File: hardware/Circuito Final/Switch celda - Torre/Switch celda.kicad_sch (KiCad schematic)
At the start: 30 parts, among them Q1 MMBT2222A, Q2 MMBT2907A, Q3 MMBT2222A

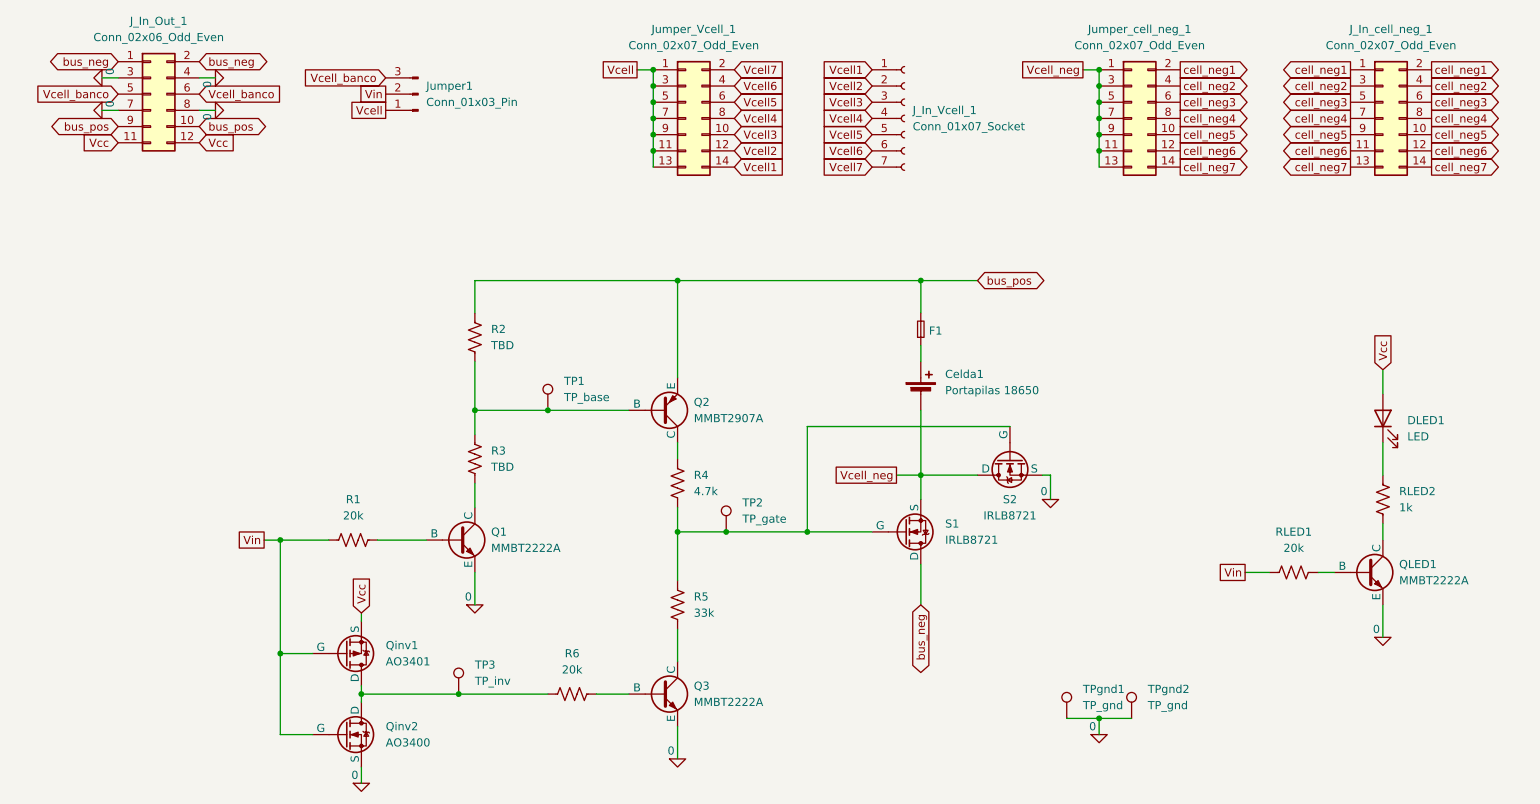
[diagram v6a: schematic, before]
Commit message: Eliminación del pin de señal de control para todo el banco y correcciones menores a la placa
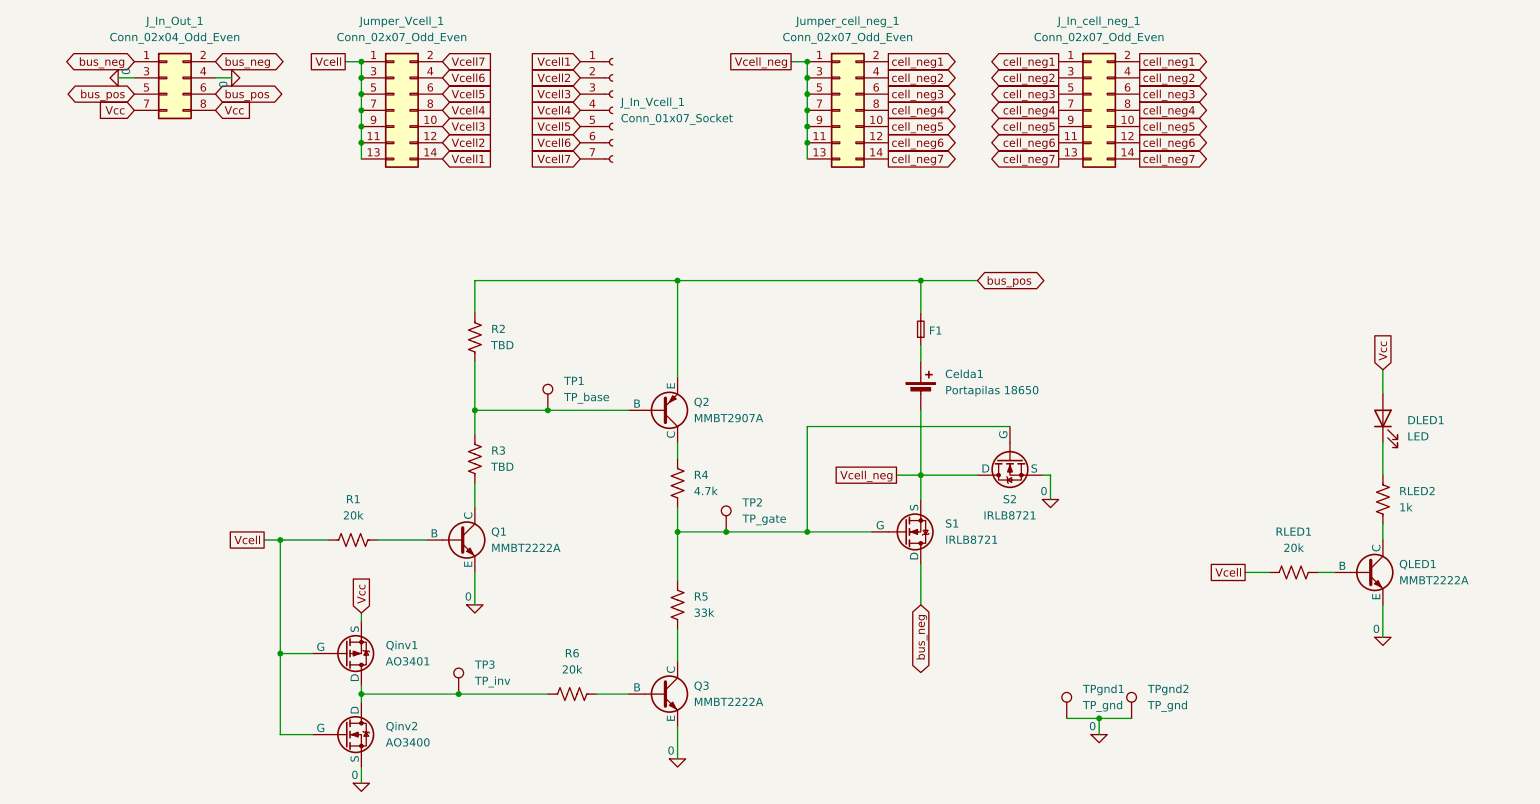
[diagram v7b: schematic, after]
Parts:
- removed J_In_Out_1: Conn_02x06_Odd_Even, Connector_PinSocket_2.54mm:PinSocket_2x06_P2.54mm_Vertical, symbol Connector_Generic:Conn_02x06_Odd_Even
- removed Jumper1: Conn_01x03_Pin, Connector_PinHeader_2.54mm:PinHeader_1x03_P2.54mm_Vertical, symbol Connector:Conn_01x03_Pin
- added J_In_Out_1: Conn_02x04_Odd_Even, Connector_PinSocket_2.54mm:PinSocket_2x04_P2.54mm_Vertical, symbol Connector_Generic:Conn_02x04_Odd_Even
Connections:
- net Vin is gone; now on net Vcell: Qinv1.2 (G), Qinv2.2 (G), R1.1, RLED1.1
- net 0: now also J_In_Out_1.3 (Pin_3), J_In_Out_1.4 (Pin_4)
- net Vcc: now also J_In_Out_1.7 (Pin_7), J_In_Out_1.8 (Pin_8)
- net bus_neg: now also J_In_Out_1.1 (Pin_1), J_In_Out_1.2 (Pin_2)
- net bus_pos: now also J_In_Out_1.5 (Pin_5), J_In_Out_1.6 (Pin_6)
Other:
- moved on the sheet: J_In_Vcell_1, J_In_cell_neg_1, Jumper_Vcell_1, Jumper_cell_neg_1

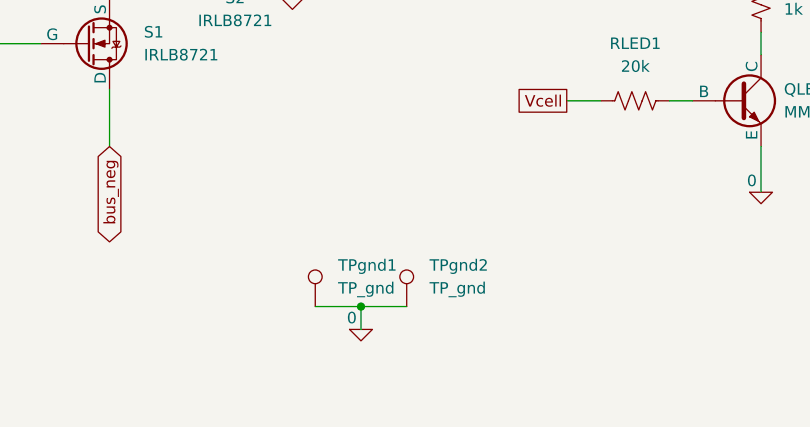
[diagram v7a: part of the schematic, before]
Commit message: Reemplazo de la vía por un resistor SMD de 0 ohm y corrección de los errores de DRC
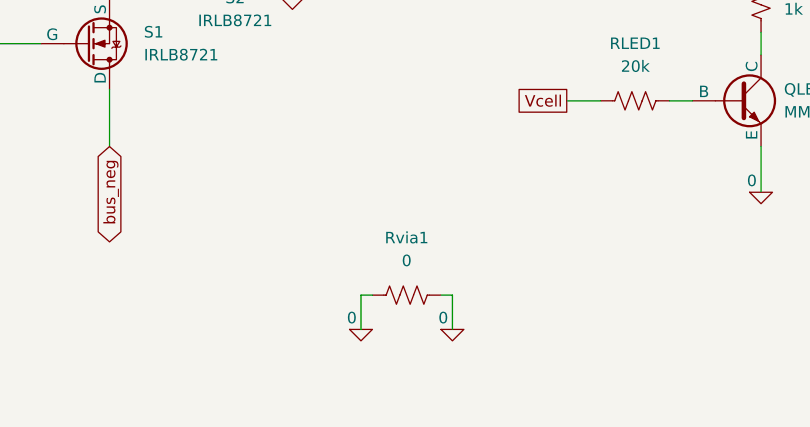
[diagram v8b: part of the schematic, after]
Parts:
- removed TPgnd1, TPgnd2: TP_gnd, Connector_PinHeader_2.54mm:PinHeader_1x01_P2.54mm_Vertical, symbol Connector:TestPoint
- added Rvia1: 0, Resistor_SMD:R_1206_3216Metric_Pad1.30x1.75mm_HandSolder, symbol Device:R_US
- F1: value ~ -> (none)
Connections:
- net 0: now also Rvia1.1, Rvia1.2
